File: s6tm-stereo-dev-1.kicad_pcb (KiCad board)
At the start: 4 copper layers, 191 parts, among them J1 Micro_SD_Card_Det1, J2 Conn_01x04_Pin, J3 USB_C_Receptacle_USB2.0_14P, J4 Conn_01x02, J5 AudioJack4, J6 Conn_01x02, J7 Conn_01x02, J8 Conn_01x02, Q1 Q_NMOS, Q2 Q_NMOS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

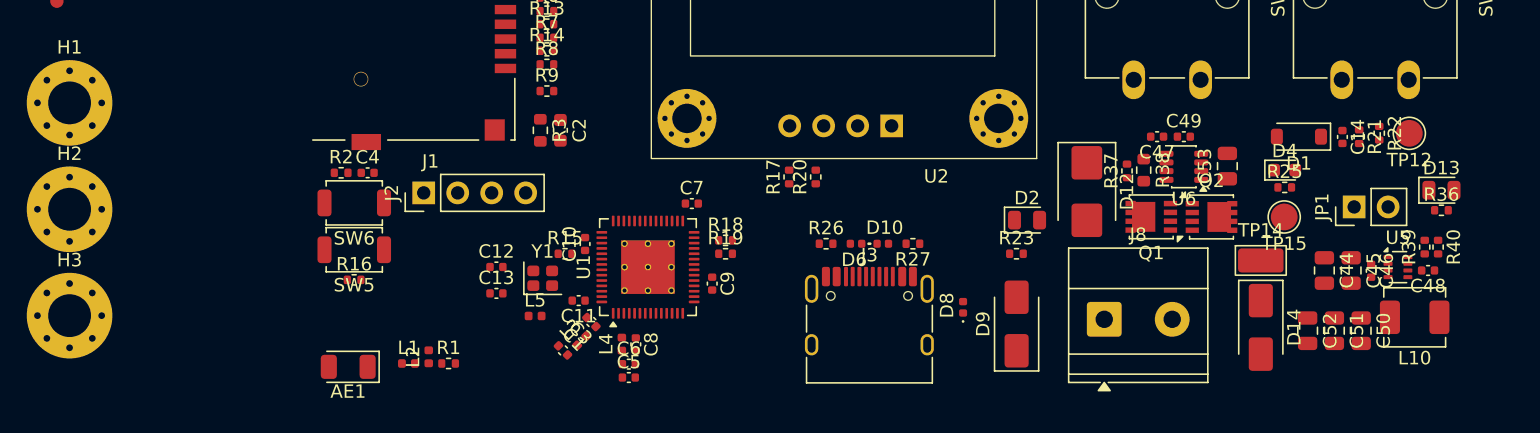
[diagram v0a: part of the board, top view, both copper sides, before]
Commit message: pcb: rpp and smps layout refinement
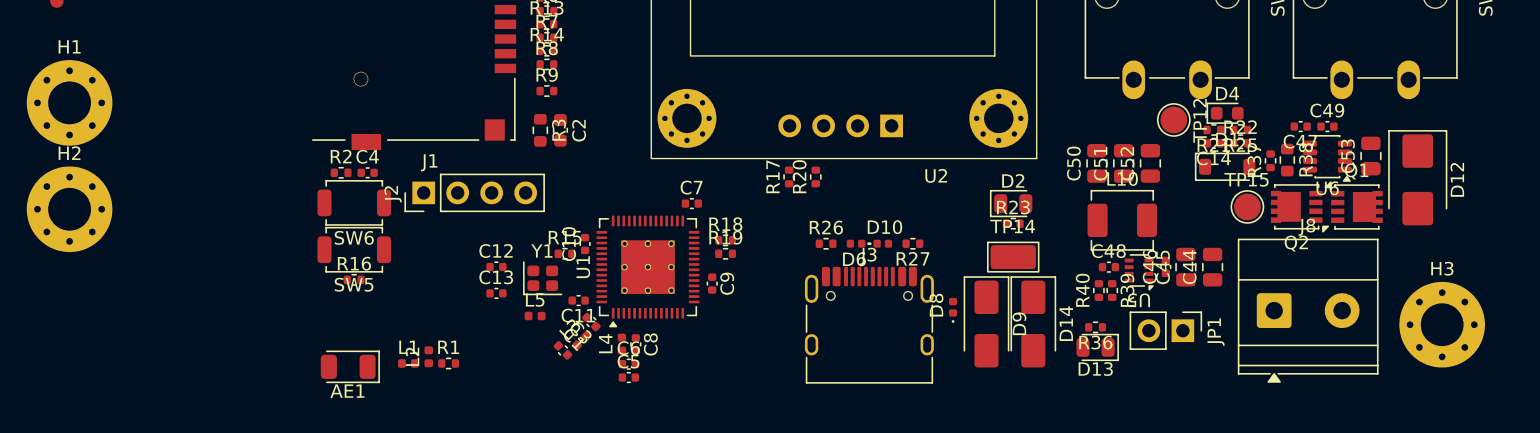
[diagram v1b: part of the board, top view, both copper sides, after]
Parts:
- moved H3 102.6 mm to (127.8, 183.1)
- moved D13 28.4 mm to (101.9, 184.8), turned to 180 degrees
- moved R36 27.3 mm to (101.9, 183.2), turned to 180 degrees
- moved R40 25.6 mm to (102.2, 180.5), turned to 90 degrees
- moved D12 24.7 mm to (126.0, 172.2)
- moved C48 23.9 mm to (102.9, 178.8), turned to 0 degrees
- moved R39 23.6 mm to (103.2, 180.5), turned to -90 degrees
- moved C50 23.4 mm to (102.0, 171.0), turned to 90 degrees
- moved L10 23.0 mm to (103.9, 175.2), turned to 0 degrees
- moved C51 20.1 mm to (104.0, 171.0), turned to 90 degrees
- moved U5 19.4 mm to (105.2, 179.0), turned to 180 degrees
- moved TP14 18.5 mm to (95.8, 178.0)
- moved TP12 17.6 mm to (107.8, 167.8), turned to -90 degrees
- moved C52 17.2 mm to (106.0, 171.0), turned to 90 degrees
- moved D14 17.0 mm to (97.2, 183.0)
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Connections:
- J8 pad 1: +Vin -> GND
- J8 pad 2: GND -> +Vin

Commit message: pcb: add audio layout
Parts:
- removed TP15: TestPoint, TestPoint:TestPoint_Pad_D2.0mm
- C32, C33: value 10u -> 1u; footprint Capacitor_SMD:C_0805_2012Metric -> Capacitor_SMD:C_0402_1005Metric
- moved H2 113.0 mm to (122.3, 116.8)
- moved SW1 80.0 mm to (124.5, 136.8), turned to 90 degrees
- moved TP3 73.7 mm to (116.5, 134.0), turned to -90 degrees
- moved TP4 69.1 mm to (113.0, 134.0), turned to -90 degrees
- moved MK1 65.3 mm to (122.3, 124.5), turned to -90 degrees
- moved J6 65.0 mm to (45.0, 132.2), turned to 90 degrees
- moved L6 63.1 mm to (67.8, 133.7)
- moved C22 62.7 mm to (113.2, 111.2), turned to 90 degrees
- moved TP5 61.4 mm to (106.2, 134.0), turned to 90 degrees
- moved TP8 61.3 mm to (109.0, 134.0), turned to 90 degrees
- moved L7 61.3 mm to (56.8, 131.0)
- moved C20 60.3 mm to (111.2, 111.2), turned to 90 degrees
- moved H1 60.3 mm to (45.9, 109.8)
- moved C19 58.0 mm to (109.2, 111.2), turned to 90 degrees
- moved C17 56.8 mm to (109.2, 114.9), turned to 90 degrees
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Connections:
- C21 pad 1: Net-(U3-HPL) -> /Amplifier/HPL
- C21 pad 2: /Amplifier/HPL -> Net-(C21-Pad2)
- C23 pad 1: Net-(U3-HPR) -> /Amplifier/HPR
- C23 pad 2: /Amplifier/HPR -> Net-(C23-Pad2)
- J5 pad R1: /Amplifier/HPR -> Net-(C23-Pad2)
- J5 pad T: /Amplifier/HPL -> Net-(C21-Pad2)
- U3 pad 27: Net-(U3-HPL) -> /Amplifier/HPL
- U3 pad 30: Net-(U3-HPR) -> /Amplifier/HPR

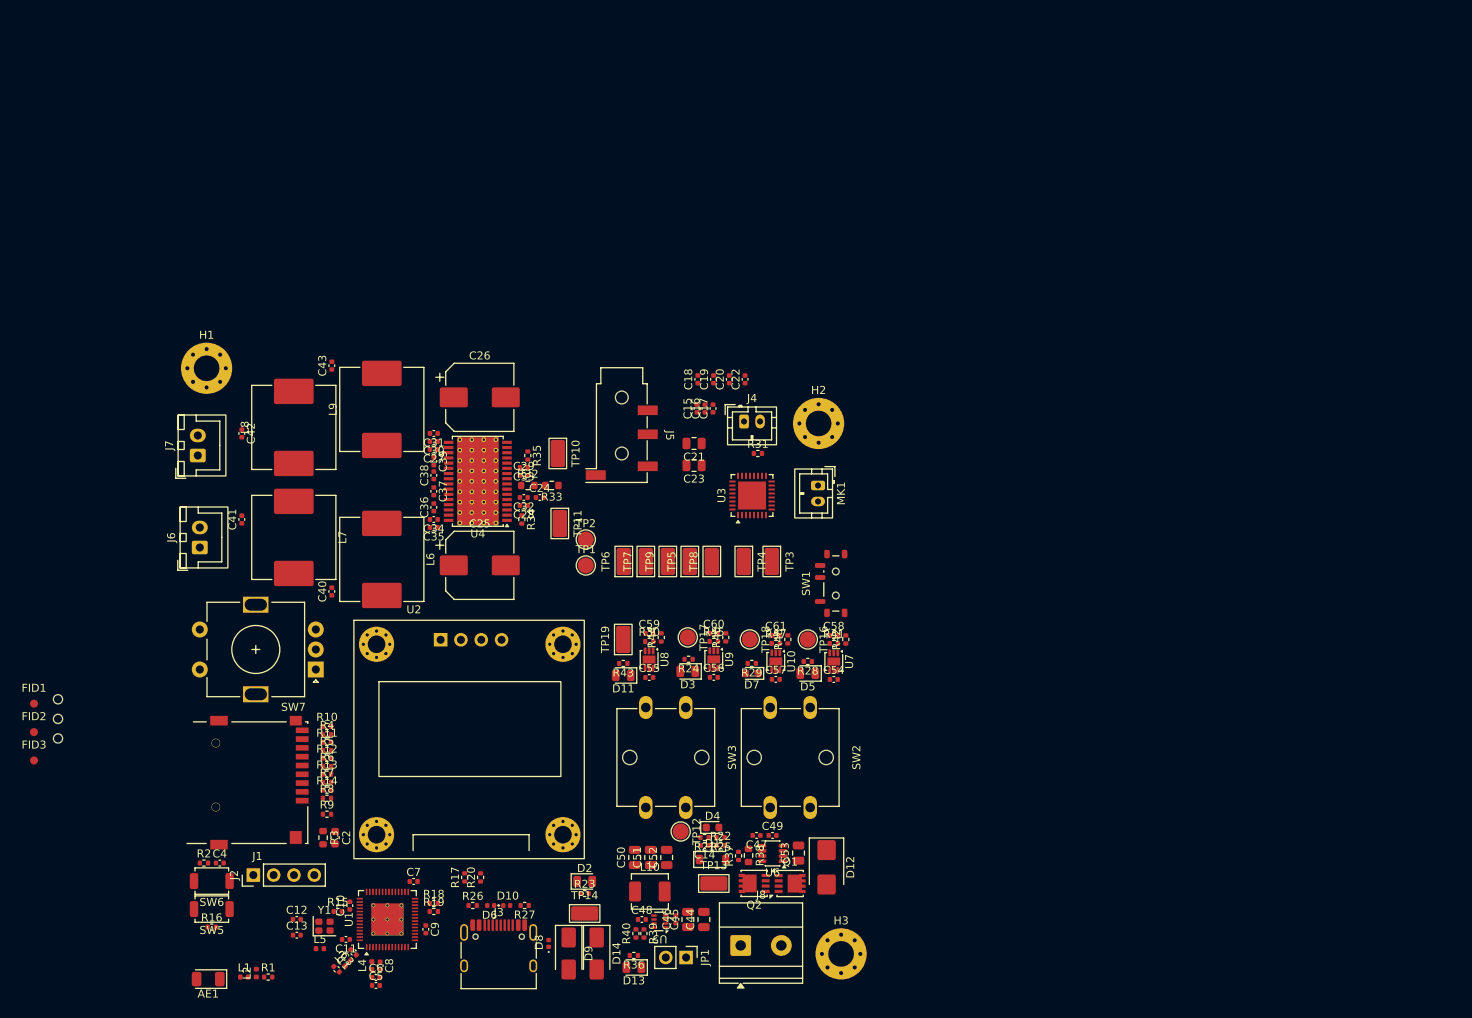
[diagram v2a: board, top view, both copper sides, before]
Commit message: pcb: refine amplifier layout
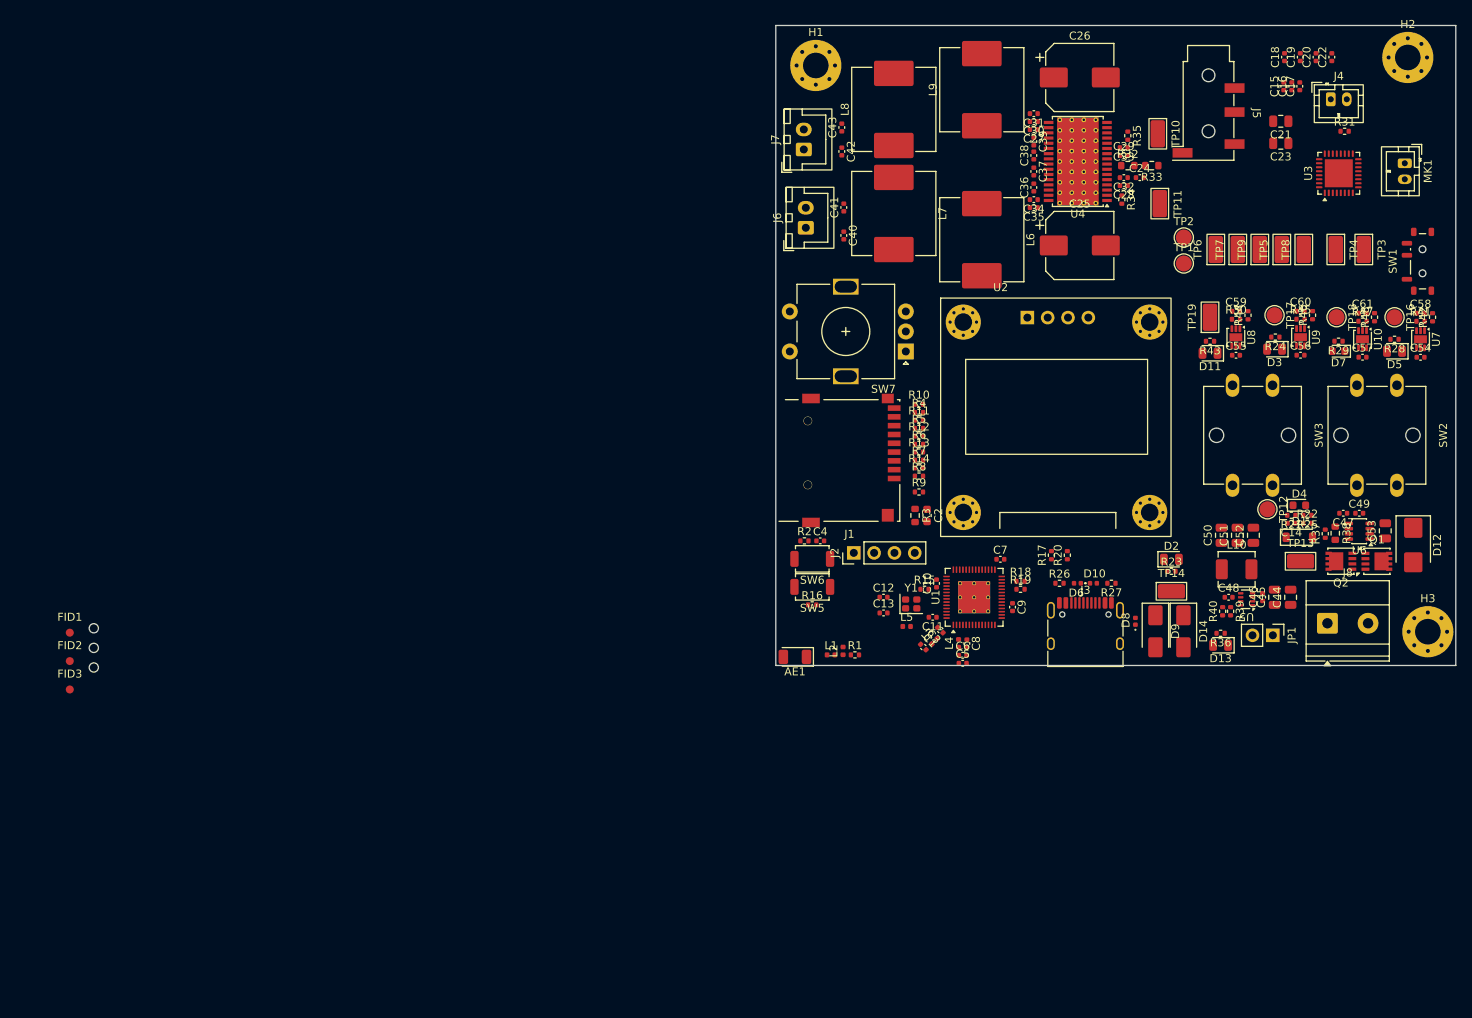
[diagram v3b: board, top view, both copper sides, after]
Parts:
- moved H2 86.7 mm to (196.0, 71.0)
- moved J6 85.6 mm to (120.8, 92.3)
- moved L7 85.2 mm to (131.8, 90.5)
- moved C4 85.2 mm to (122.6, 131.4)
- moved J2 85.2 mm to (126.8, 132.9)
- moved R16 85.2 mm to (121.5, 139.4)
- moved R2 85.2 mm to (120.6, 131.4)
- moved SW5 85.2 mm to (121.6, 137.2)
- moved SW6 85.2 mm to (121.6, 133.7)
- moved H1 85.0 mm to (122.0, 72.0)
- moved C24 85.0 mm to (162.5, 86.0)
- moved C25 85.0 mm to (155.0, 94.5)
- moved C26 85.0 mm to (155.0, 73.5)
- moved C27 85.0 mm to (149.2, 80.0)
- moved C28 85.0 mm to (160.5, 87.0)
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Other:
- board outline added: 85 x 80 mm

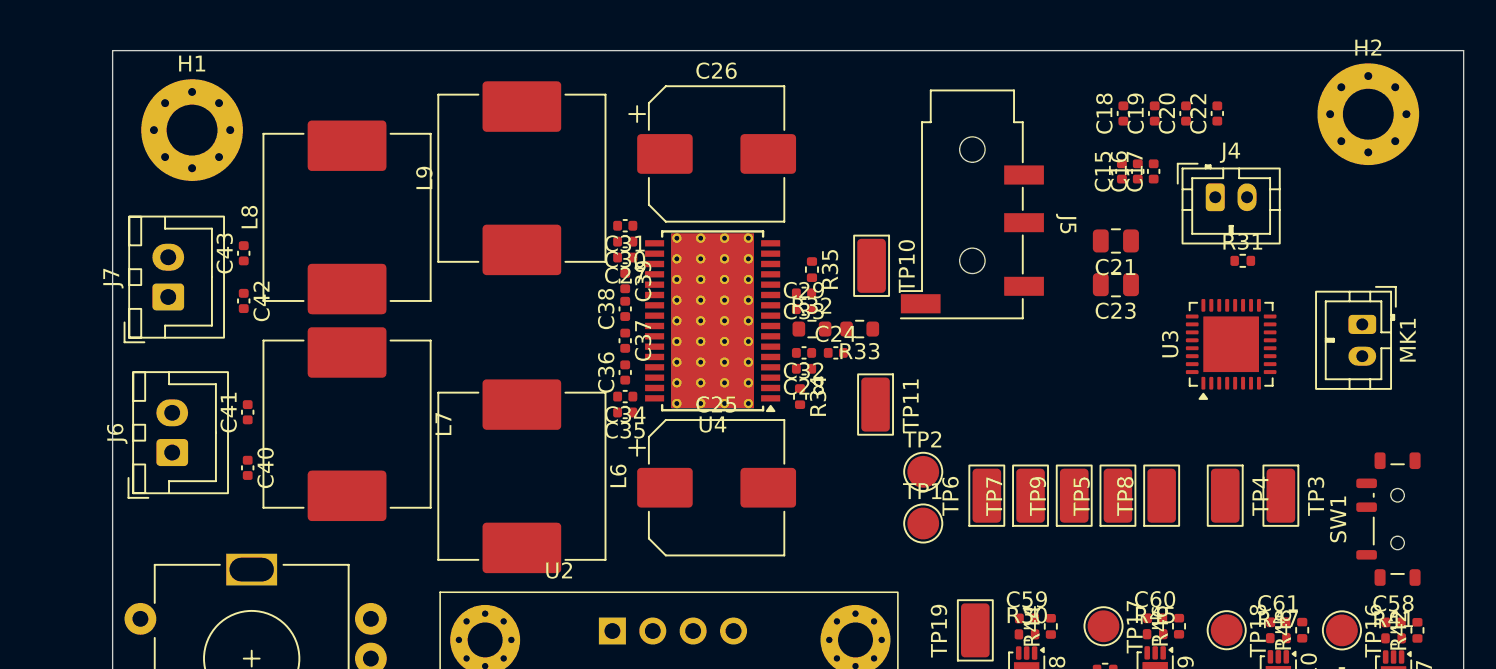
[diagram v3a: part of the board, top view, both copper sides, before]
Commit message: pcb: refine codec layout
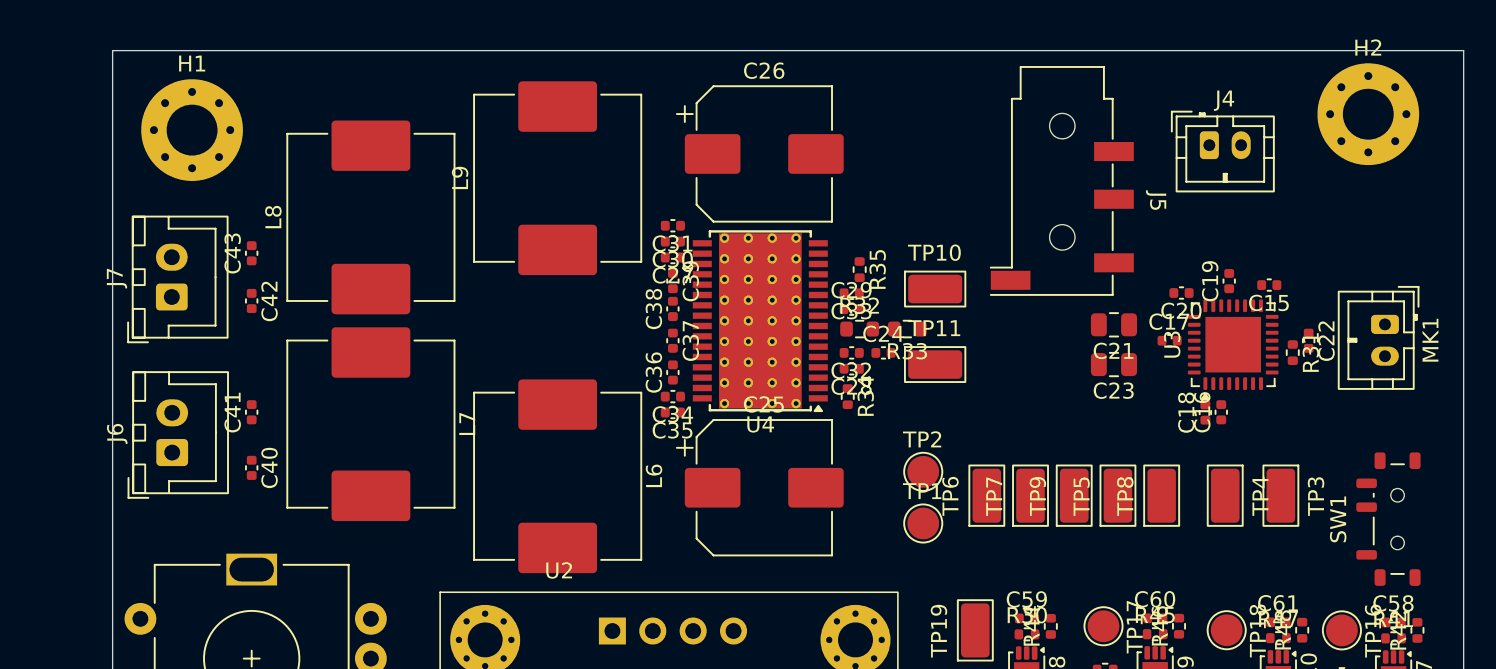
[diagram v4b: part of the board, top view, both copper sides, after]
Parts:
- moved C18 19.5 mm to (185.8, 89.8)
- moved C16 16.0 mm to (186.8, 89.8)
- moved C22 15.4 mm to (192.2, 85.2), turned to -90 degrees
- moved C15 11.7 mm to (189.8, 81.8), turned to 180 degrees
- moved C19 11.5 mm to (187.2, 81.5)
- moved C20 11.3 mm to (184.2, 82.2), turned to 180 degrees
- moved C17 10.7 mm to (183.5, 85.2), turned to 0 degrees
- moved R31 6.58 mm to (191.2, 86.0), turned to -90 degrees
- moved J5 5.85 mm to (176.8, 76.5)
- moved C21 5.28 mm to (180.0, 84.2)
- moved C23 5.03 mm to (180.0, 86.8)
- moved TP11 4.52 mm to (168.8, 86.8), turned to 0 degrees
- moved TP10 4.26 mm to (168.8, 82.0), turned to 0 degrees
- moved J4 3.30 mm to (186.0, 73.0)
- moved C24 3.00 mm to (165.5, 86.0)
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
